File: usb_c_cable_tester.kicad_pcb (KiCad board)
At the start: 2 copper layers, 85.6 x 54 mm, 58 parts, among them J1 USB C, J2 USB C, J3 USB_B_Micro, J4 USB3_B, J5 USB_B_Mini, J6 USB3_A

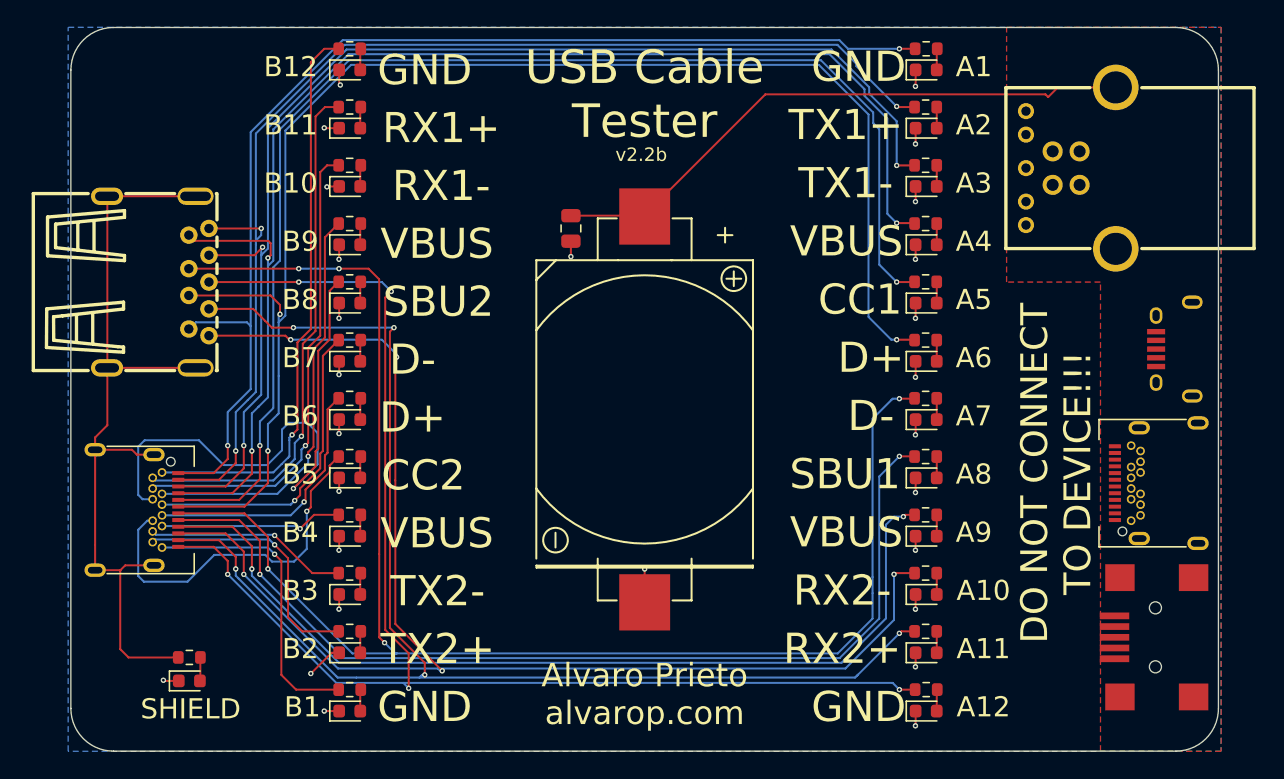
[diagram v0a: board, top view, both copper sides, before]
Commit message: Revert "Merging changes for current (2026 May) JLCPCB stock and ordering."
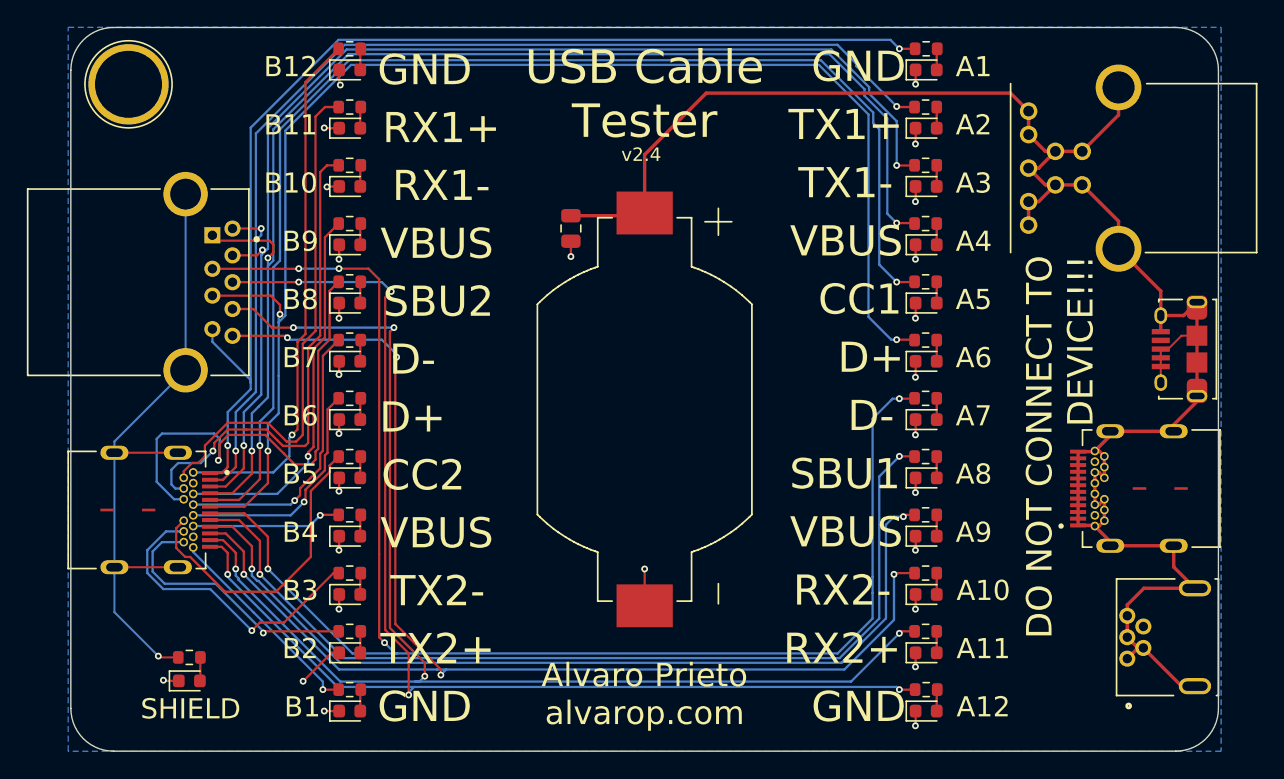
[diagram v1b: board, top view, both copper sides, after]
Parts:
- added REF**: TestPoint_Plated_Hole_D5.0mm, TestPoint:TestPoint_Plated_Hole_D5.0mm, F.Cu at (61.5, 77.2)
- added REF**: OSHW-Logo_11.4x12mm_SilkScreen, Symbol:OSHW-Logo_11.4x12mm_SilkScreen, B.Cu at (100.2, 81.0)
- BT1: footprint easyeda:BAT-TH_CR2032-BS-6-1 -> snapeda:BAT_BU2032SM-BT-GTR
- C1: value C_Small -> 1uF
- J1, J2: value USB C -> USB_C_Receptacle; footprint Libraries:USB_C_Receptacle_24P_QCHT_C456013 -> snapeda:BELFUSE_SS-52400-003
- J3: footprint easyeda:MICRO-USB-SMD_10118194-0001LF -> snapeda:AMPHENOL_10118194-0001LF_MOD
- J4: footprint easyeda:USB-B-TH_XUNPU_USB-306BWD-ARW -> snapeda:AMPHENOL_GSB3211311WEU
- J5: footprint easyeda:MINI-USB-SMD_MINI-5PTP -> snapeda:TE_1734510-1
- J6: footprint easyeda:USB-A-TH_U231-091N-5 -> snapeda:AMPHENOL_GSB311131HR
- R1, R10, R11, R12, R13, R14, R15, R16, R17, R18, R19, R2, R20, R21, R22, R23, R24, R25, R3, R4, R5, R6, R7, R8, R9: value 1k -> 330
- moved J6 4.06 mm to (67.8, 92.0)
- moved J4 3.56 mm to (135.3, 83.5)
- moved J5 3.05 mm to (141.1, 118.5)
- moved J3 1.70 mm to (141.2, 97.0)
- moved J1 0.67 mm to (139.5, 107.4)
- moved J2 0.16 mm to (60.5, 109.0)
- turned BT1 to -90 degrees
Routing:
- net +3V3: track 44.8 -> 146.9 mm
- net /SHLD: track 61.8 -> 49.0 mm, vias 0 -> 1
- net /TX2-: track 15.2 -> 22.8 mm
- net /SBU2: track 43.4 -> 36.2 mm
- net /GND_B1: track 22.5 -> 15.8 mm
- net /TX1-: track 92.9 -> 88.5 mm
- net /D+_A: track 109.0 -> 104.9 mm
- net /D-_A: track 120.3 -> 116.2 mm
- net /TX1+: track 88.9 -> 84.9 mm
- net /VBUS_A4: track 100.4 -> 96.5 mm
- net /CC2: track 26.9 -> 23.1 mm, vias 1 -> 0
- net /RX2-: track 105.1 -> 101.5 mm
- net /RX2+: track 103.5 -> 100.2 mm
- net /GND_B12: track 42.5 -> 39.6 mm
- net /GND_A12: track 104.9 -> 102.1 mm
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- removed copper zone on F.Cu, net +3V3
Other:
- board text added: "Connect USB cable to both sides of the board. The LED of each connected signal will light up."
- board text added: "v${REVISION}"
- board text removed: "Connect USB cable to both sides of the board The LED of each connected signal will light up"
- board text removed: "v2.2b"
